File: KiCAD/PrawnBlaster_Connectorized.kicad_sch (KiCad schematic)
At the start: 25 parts, among them IC1 74LVT245D,118, J1 Conn_Coaxial, J2 Conn_Coaxial, J3 Conn_Coaxial, J4 Conn_Coaxial, J5 Conn_Coaxial, J6 Conn_Coaxial, U1 74LVC1G07, U2 Pico, U3 74LVC1G17

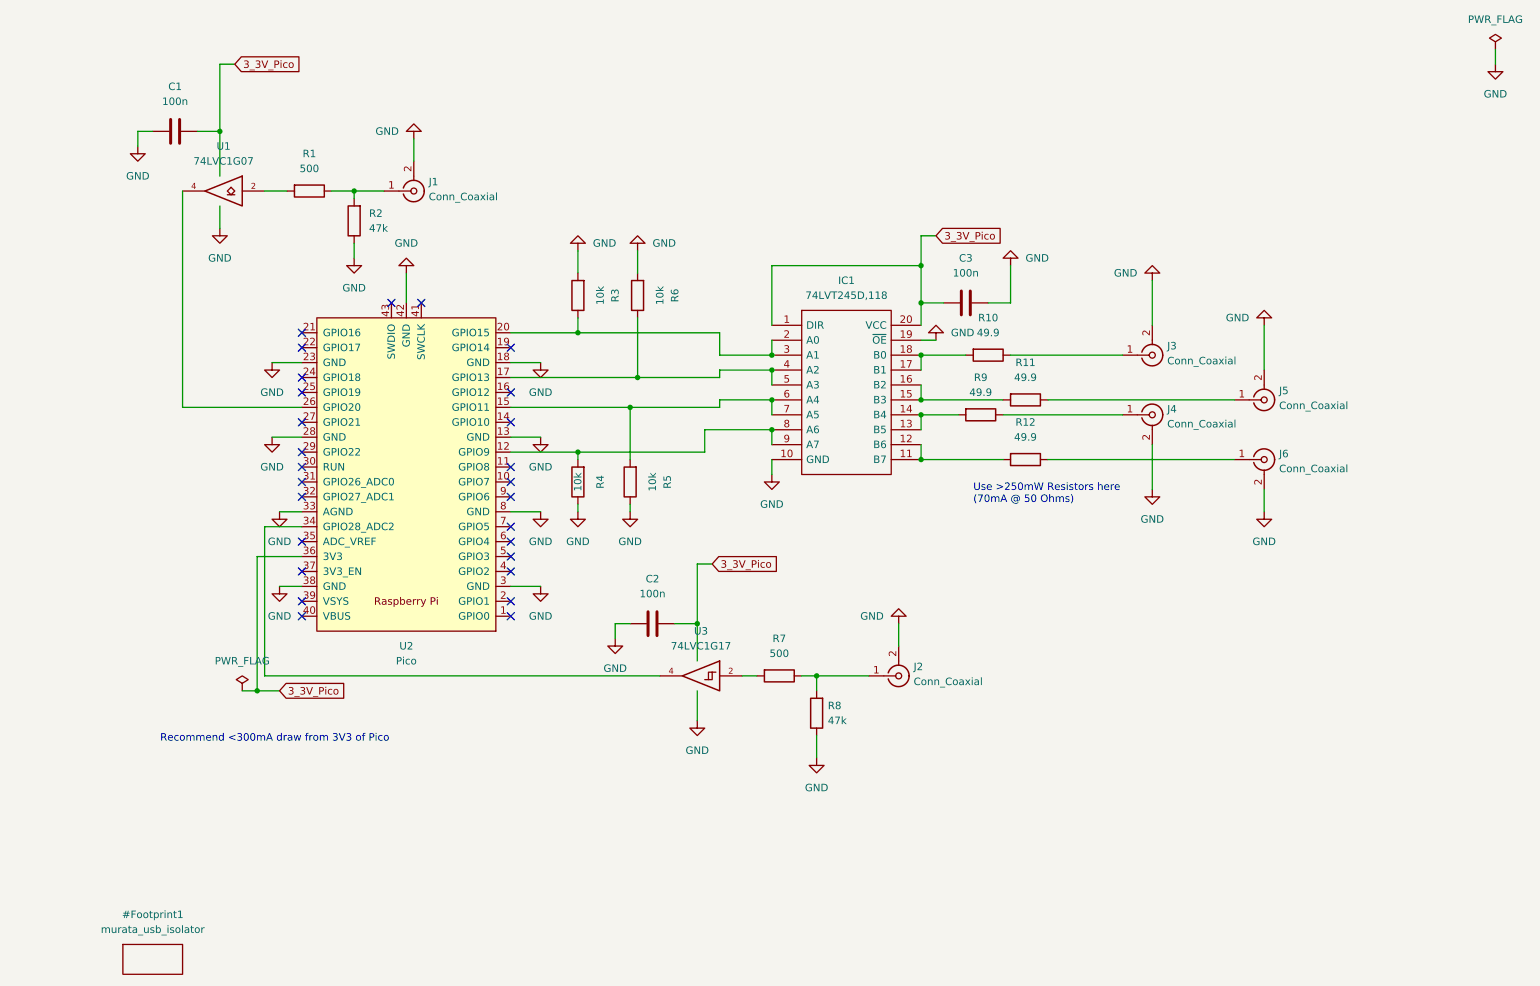
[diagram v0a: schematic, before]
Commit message: Update trigger GPIO to 22. Add internal clock testpoints. Add updated labels to silkscreen. Add mounting holes.
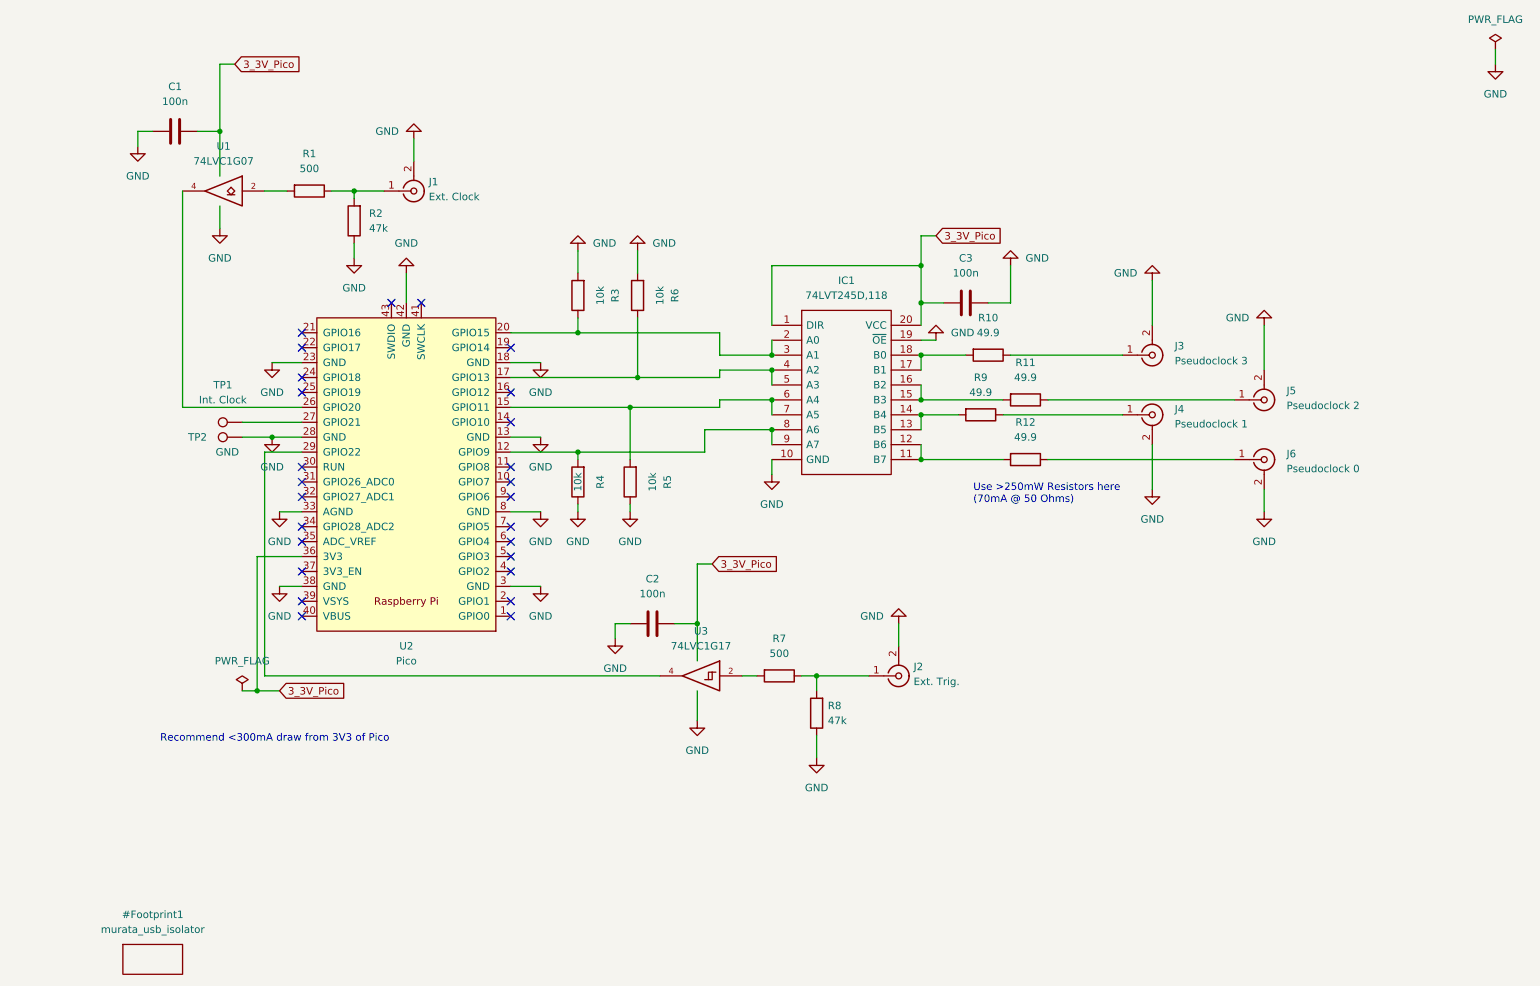
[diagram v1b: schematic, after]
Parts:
- added TP1: Int. Clock, TestPoint:TestPoint_Pad_1.0x1.0mm, symbol Connector:TestPoint
- added TP2: GND, TestPoint:TestPoint_Pad_1.0x1.0mm, symbol Connector:TestPoint
- J1: value Conn_Coaxial -> Ext. Clock
- J2: value Conn_Coaxial -> Ext. Trig.
- J3: value Conn_Coaxial -> Pseudoclock 3
- J4: value Conn_Coaxial -> Pseudoclock 1
- J5: value Conn_Coaxial -> Pseudoclock 2
- J6: value Conn_Coaxial -> Pseudoclock 0
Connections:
- net GND: now also TP2.1
- net at U3.4: now also U2.29 (GPIO22); no longer U2.34 (GPIO28_ADC2)
- net at U2.27 (GPIO21): now also TP1.1
- no-connect marks 27 -> 26
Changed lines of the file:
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@@
   (junction (at 153.67 129.54) (diameter 0) (color 0 0 0 0)
+  )
+  (junction (at 60.96 88.9) (diameter 0) (color 0 0 0 0)
   )
   (junction (at 146.05 74.93) (diameter 0) (color 0 0 0 0)
@@
   (no_connect (at 66.04 116.84))
   (no_connect (at 66.04 119.38))
-  (no_connect (at 66.04 91.44))
-  (no_connect (at 66.04 86.36))
   (no_connect (at 66.04 111.76))
   (no_connect (at 66.04 106.68))
+  (no_connect (at 66.04 104.14))
   (wire (pts (xy 146.05 77.47) (xy 146.05 80.01))
     (stroke (width 0) (type default) (color 0 0 0 0))
@@
     (stroke (width 0) (type default) (color 0 0 0 0))
   )
+  (wire (pts (xy 59.69 91.44) (xy 66.04 91.44))
+    (stroke (width 0) (type default) (color 0 0 0 0))
+  )
   (wire (pts (xy 146.05 59.69) (xy 171.45 59.69))
     (stroke (width 0) (type default) (color 0 0 0 0))
@@
     (stroke (width 0) (type default) (color 0 0 0 0))
   )
-  (wire (pts (xy 59.69 104.14) (xy 66.04 104.14))
-    (stroke (width 0) (type default) (color 0 0 0 0))
-  )
   (wire (pts (xy 123.19 68.58) (xy 123.19 78.74))
     (stroke (width 0) (type default) (color 0 0 0 0))
@@
     (stroke (width 0) (type default) (color 0 0 0 0))
   )
+  (wire (pts (xy 55.88 88.9) (xy 60.96 88.9))
+    (stroke (width 0) (type default) (color 0 0 0 0))
+  )
   (wire (pts (xy 137.16 83.82) (xy 137.16 82.55))
     (stroke (width 0) (type default) (color 0 0 0 0))
@@
     (stroke (width 0) (type default) (color 0 0 0 0))
   )
-  (wire (pts (xy 59.69 129.54) (xy 59.69 104.14))
+  (wire (pts (xy 59.69 91.44) (xy 59.69 129.54))
     (stroke (width 0) (type default) (color 0 0 0 0))
   )
@@
   )
   (wire (pts (xy 133.35 110.49) (xy 135.89 110.49))
+    (stroke (width 0) (type default) (color 0 0 0 0))
+  )
+  (wire (pts (xy 55.88 86.36) (xy 66.04 86.36))
     (stroke (width 0) (type default) (color 0 0 0 0))
   )
@@
       (effects (font (size 1.27 1.27)) (justify left))
     )
-    (property "Value" "Conn_Coaxial" (id 1) (at 87.63 47.9667 0)
+    (property "Value" "Ext. Clock" (id 1) (at 87.63 47.9667 0)
       (effects (font (size 1.27 1.27)) (justify left))
     )
@@
     (pin "1")
   )
+  (symbol (lib_id "Connector:TestPoint") (at 55.88 88.9 90) (unit 1)
+    (in_bom yes) (on_board yes)
+    (property "Reference" "TP2" (id 0) (at 48.26 88.9 90))
+    (property "Value" "GND" (id 1) (at 53.34 91.44 90))
+    (property "Footprint" "TestPoint:TestPoint_Pad_1.0x1.0mm" (id 2) (at 55.88 83.82 0)
+      (effects (font (size 1.27 1.27)) hide)
+    )
+    (property "Datasheet" "~" (id 3) (at 55.88 83.82 0)
+      (effects (font (size 1.27 1.27)) hide)
+    )
+    (pin "1")
+  )
   (symbol (lib_id "power:GND") (at 119.38 123.19 0) (unit 1)
     (in_bom yes) (on_board yes) (fields_autoplaced)
@@
   (symbol (lib_id "Connector:Conn_Coaxial") (at 210.82 85.09 0) (unit 1)
     (in_bom yes) (on_board yes) (fields_autoplaced)
-    (property "Reference" "J4" (id 0) (at 213.36 84.1131 0)
+    (property "Reference" "J4" (id 0) (at 214.63 84.1131 0)
       (effects (font (size 1.27 1.27)) (justify left))
     )
-    (property "Value" "Conn_Coaxial" (id 1) (at 213.36 86.6531 0)
+    (property "Value" "Pseudoclock 1" (id 1) (at 214.63 86.6531 0)
       (effects (font (size 1.27 1.27)) (justify left))
     )
@@
   (symbol (lib_id "Connector:Conn_Coaxial") (at 229.87 92.71 0) (unit 1)
     (in_bom yes) (on_board yes) (fields_autoplaced)
-    (property "Reference" "J6" (id 0) (at 232.41 91.7331 0)
+    (property "Reference" "J6" (id 0) (at 233.68 91.7331 0)
       (effects (font (size 1.27 1.27)) (justify left))
     )
-    (property "Value" "Conn_Coaxial" (id 1) (at 232.41 94.2731 0)
+    (property "Value" "Pseudoclock 0" (id 1) (at 233.68 94.2731 0)
       (effects (font (size 1.27 1.27)) (justify left))
     )
@@
   (symbol (lib_id "Connector:Conn_Coaxial") (at 210.82 74.93 0) (mirror x) (unit 1)
     (in_bom yes) (on_board yes) (fields_autoplaced)
-    (property "Reference" "J3" (id 0) (at 213.36 73.3667 0)
+    (property "Reference" "J3" (id 0) (at 214.63 73.3667 0)
       (effects (font (size 1.27 1.27)) (justify left))
     )
-    (property "Value" "Conn_Coaxial" (id 1) (at 213.36 75.9067 0)
+    (property "Value" "Pseudoclock 3" (id 1) (at 214.63 75.9067 0)
       (effects (font (size 1.27 1.27)) (justify left))
     )
@@
       (effects (font (size 1.27 1.27)) (justify left))
     )
-    (property "Value" "Conn_Coaxial" (id 1) (at 170.18 130.5167 0)
+    (property "Value" "Ext. Trig." (id 1) (at 170.18 130.5167 0)
       (effects (font (size 1.27 1.27)) (justify left))
     )
@@
   (symbol (lib_id "Connector:Conn_Coaxial") (at 229.87 82.55 0) (mirror x) (unit 1)
     (in_bom yes) (on_board yes) (fields_autoplaced)
-    (property "Reference" "J5" (id 0) (at 232.41 80.9867 0)
+    (property "Reference" "J5" (id 0) (at 233.68 80.9867 0)
       (effects (font (size 1.27 1.27)) (justify left))
     )
-    (property "Value" "Conn_Coaxial" (id 1) (at 232.41 83.5267 0)
+    (property "Value" "Pseudoclock 2" (id 1) (at 233.68 83.5267 0)
       (effects (font (size 1.27 1.27)) (justify left))
     )
@@
     (pin "9")
   )
+  (symbol (lib_id "Connector:TestPoint") (at 55.88 86.36 90) (unit 1)
+    (in_bom yes) (on_board yes) (fields_autoplaced)
+    (property "Reference" "TP1" (id 0) (at 52.578 80.01 90))
+    (property "Value" "Int. Clock" (id 1) (at 52.578 82.55 90))
+    (property "Footprint" "TestPoint:TestPoint_Pad_1.0x1.0mm" (id 2) (at 55.88 81.28 0)
+      (effects (font (size 1.27 1.27)) hide)
+    )
+    (property "Datasheet" "~" (id 3) (at 55.88 81.28 0)
+      (effects (font (size 1.27 1.27)) hide)
+    )
+    (pin "1")
+  )
   (symbol (lib_id "power:GND") (at 153.67 143.51 0) (unit 1)
     (in_bom yes) (on_board yes) (fields_autoplaced)
@@
     )
     (path "/0d26cb14-4684-4c8e-8750-fd3cf3ffdeb1"
-      (reference "J1") (unit 1) (value "Conn_Coaxial") (footprint "Connector_Coaxial:SMA_Amphenol_132289_EdgeMount")
+      (reference "J1") (unit 1) (value "Ext. Clock") (footprint "Connector_Coaxial:SMA_Amphenol_132289_EdgeMount")
     )
     (path "/cd33b516-8d7f-4ef6-9602-21d81c0beb81"
-      (reference "J2") (unit 1) (value "Conn_Coaxial") (footprint "Connector_Coaxial:SMA_Amphenol_132289_EdgeMount")
+      (reference "J2") (unit 1) (value "Ext. Trig.") (footprint "Connector_Coaxial:SMA_Amphenol_132289_EdgeMount")
     )
     (path "/c2c761fe-8f1e-496b-90f9-74f8cf2965f1"
-      (reference "J3") (unit 1) (value "Conn_Coaxial") (footprint "Connector_Coaxial:SMA_Amphenol_132289_EdgeMount")
+      (reference "J3") (unit 1) (value "Pseudoclock 3") (footprint "Connector_Coaxial:SMA_Amphenol_132289_EdgeMount")
     )
     (path "/857cdcea-516d-4c1f-9bee-a56a3e14e2f2"
-      (reference "J4") (unit 1) (value "Conn_Coaxial") (footprint "Connector_Coaxial:SMA_Amphenol_132289_EdgeMount")
+      (reference "J4") (unit 1) (value "Pseudoclock 1") (footprint "Connector_Coaxial:SMA_Amphenol_132289_EdgeMount")
     )
     (path "/e6cba089-3be2-4575-aa68-1802798f776e"
-      (reference "J5") (unit 1) (value "Conn_Coaxial") (footprint "Connector_Coaxial:SMA_Amphenol_132289_EdgeMount")
+      (reference "J5") (unit 1) (value "Pseudoclock 2") (footprint "Connector_Coaxial:SMA_Amphenol_132289_EdgeMount")
     )
     (path "/b81fa6df-2806-4fa5-b688-563f0f4f4616"
-      (reference "J6") (unit 1) (value "Conn_Coaxial") (footprint "Connector_Coaxial:SMA_Amphenol_132289_EdgeMount")
+      (reference "J6") (unit 1) (value "Pseudoclock 0") (footprint "Connector_Coaxial:SMA_Amphenol_132289_EdgeMount")
     )
     (path "/67b69d7f-65e7-4841-8078-c2c42d43b14a"
@@
       (reference "R12") (unit 1) (value "49.9") (footprint "Resistor_SMD:R_1206_3216Metric_Pad1.30x1.75mm_HandSolder")
     )
+    (path "/edc90777-da57-446d-a784-3913a533f8ca"
+      (reference "TP1") (unit 1) (value "Int. Clock") (footprint "TestPoint:TestPoint_Pad_1.0x1.0mm")
+    )
+    (path "/6bf43832-e440-4eaa-88c7-e6a97107d867"
+      (reference "TP2") (unit 1) (value "GND") (footprint "TestPoint:TestPoint_Pad_1.0x1.0mm")
+    )
     (path "/d8903fa4-d8a9-4284-8df6-88bda4a26782"

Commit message: Update to have internal clock output, larger logo, and new buffer chips
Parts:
- removed TP1: Int. Clock, TestPoint:TestPoint_Pad_1.0x1.0mm, symbol Connector:TestPoint
- removed TP2: GND, TestPoint:TestPoint_Pad_1.0x1.0mm, symbol Connector:TestPoint
- removed U1: 74LVC1G07, Package_TO_SOT_SMD:SOT-23-5_HandSoldering, symbol 74xGxx:74LVC1G07
- added C2: 100n, Capacitor_SMD:C_0805_2012Metric_Pad1.18x1.45mm_HandSolder, symbol Device:C
- added J1: Int. Clock, Connector_Coaxial:SMA_Amphenol_132289_EdgeMount, symbol Connector:Conn_Coaxial
- added R1: 49.9, Resistor_SMD:R_1206_3216Metric_Pad1.30x1.75mm_HandSolder, symbol Device:R
- added U1, U2: 74LVC1G34, Package_TO_SOT_SMD:SOT-23-5_HandSoldering, symbol 74xGxx:74LVC1G34
- R2: renamed from R1; footprint Resistor_SMD:R_0805_2012Metric_Pad1.20x1.40mm_HandSolder -> Resistor_SMD:R_1206_3216Metric_Pad1.30x1.75mm_HandSolder
- R8: renamed from R7; footprint Resistor_SMD:R_0805_2012Metric_Pad1.20x1.40mm_HandSolder -> Resistor_SMD:R_1206_3216Metric_Pad1.30x1.75mm_HandSolder
- renumbered C2 to C3, C3 to C4, J1 to J2, J2 to J3, J3 to J4, J4 to J5, J5 to J6, J6 to J7, R9 to R10, R10 to R11, R11 to R12, R12 to R13, R2 to R3, R3 to R4, R4 to R5, R5 to R6, R6 to R7, R8 to R9, U2 to U3, U3 to U4
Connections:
- net GND: now also C2.2, J1.2 (Ext), U1.3 (GND), U2.3 (GND)
- net at R2.2: now also U2.2
- net at U3.26 (GPIO20): now also U2.4
- net at U3.27 (GPIO21): now also U1.2
- net VCC renamed 3_3V_Pico
- net 3_3V_Pico: now also C2.1, U1.5 (VCC), U2.5 (VCC)
- new net: J1.1 (In), R1.2
- new net: R1.1, U1.4
- no-connect marks 26 -> 29
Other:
- moved on the sheet: C1, R8, R9

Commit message: Fix trigger input to be labscript default
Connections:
- net at U4.4: now also U3.1 (GPIO0); no longer U3.29 (GPIO22)

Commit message: Add reset jumper headers and make ARL logo slightly larger.
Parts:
- added JP1: Jumper_3_Open, Connector_PinHeader_2.54mm:PinHeader_1x03_P2.54mm_Vertical, symbol Jumper:Jumper_3_Open
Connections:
- net GND: now also JP1.1 (A)
- net at U3.30 (RUN): now also JP1.2 (C)
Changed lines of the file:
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@@
   (junction (at 123.19 78.74) (diameter 0) (color 0 0 0 0)
   )
+  (junction (at 62.23 101.6) (diameter 0) (color 0 0 0 0)
+  )
   (junction (at 58.42 132.08) (diameter 0) (color 0 0 0 0)
   )
+  (no_connect (at 55.88 87.63))
   (no_connect (at 66.04 91.44))
   (no_connect (at 66.04 71.12))
@@
   (no_connect (at 66.04 99.06))
   (no_connect (at 66.04 96.52))
-  (no_connect (at 66.04 93.98))
   (no_connect (at 66.04 116.84))
   (no_connect (at 66.04 119.38))
@@
     (stroke (width 0) (type default))
   )
+  (wire (pts (xy 59.69 93.98) (xy 66.04 93.98))
+    (stroke (width 0) (type default))
+  )
   (wire (pts (xy 123.19 68.58) (xy 123.19 78.74))
     (stroke (width 0) (type default))
@@
     (stroke (width 0) (type default))
   )
+  (wire (pts (xy 62.23 100.33) (xy 62.23 101.6))
+    (stroke (width 0) (type default))
+  )
   (wire (pts (xy 171.45 85.09) (xy 171.45 87.63))
     (stroke (width 0) (type default))
@@
   )
   (wire (pts (xy 137.16 74.93) (xy 146.05 74.93))
+    (stroke (width 0) (type default))
+  )
+  (wire (pts (xy 55.88 100.33) (xy 62.23 100.33))
     (stroke (width 0) (type default))
   )
@@
         )
       )
+    )
+  )
+  (symbol (lib_id "Jumper:Jumper_3_Open") (at 55.88 93.98 90) (unit 1)
+    (in_bom yes) (on_board yes) (dnp no) (fields_autoplaced)
+    (property "Reference" "JP1" (at 53.34 92.71 90)
+      (effects (font (size 1.27 1.27)) (justify left))
+    )
+    (property "Value" "Jumper_3_Open" (at 53.34 95.25 90)
+      (effects (font (size 1.27 1.27)) (justify left))
+    )
+    (property "Footprint" "Connector_PinHeader_2.54mm:PinHeader_1x03_P2.54mm_Vertical" (at 55.88 93.98 0)
+      (effects (font (size 1.27 1.27)) hide)
+    )
+    (property "Datasheet" "~" (at 55.88 93.98 0)
+      (effects (font (size 1.27 1.27)) hide)
+    )
+    (pin "1")
+    (pin "2")
+    (pin "3")
+    (instances
+      (project "PrawnBlaster_Connectorized"
+        (path "/aa2b0f9c-998a-4cca-8380-404df994482a"
+          (reference "JP1") (unit 1)
+        )
+      )
